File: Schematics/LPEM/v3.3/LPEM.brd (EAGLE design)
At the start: 55.5 x 99.1 mm, 40 parts, among them IC1 7805, IC2 PCA9600SO8, IC3 7803, IC4 7810, Q1 12MHz, U1 STM32F303K8T6, U2 MAX3421E

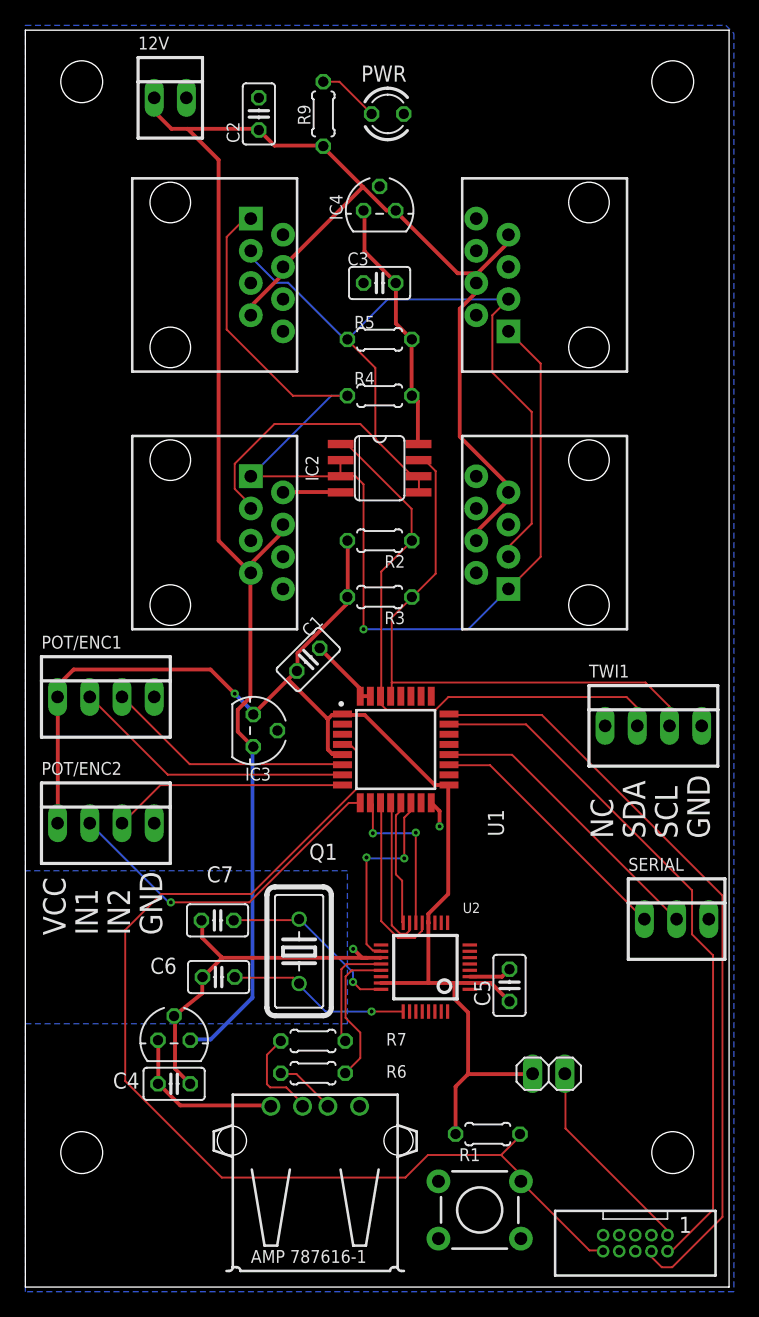
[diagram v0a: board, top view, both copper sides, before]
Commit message: Add LPEM v3.3, which will probably never be produced, and a few cleanups to other files.
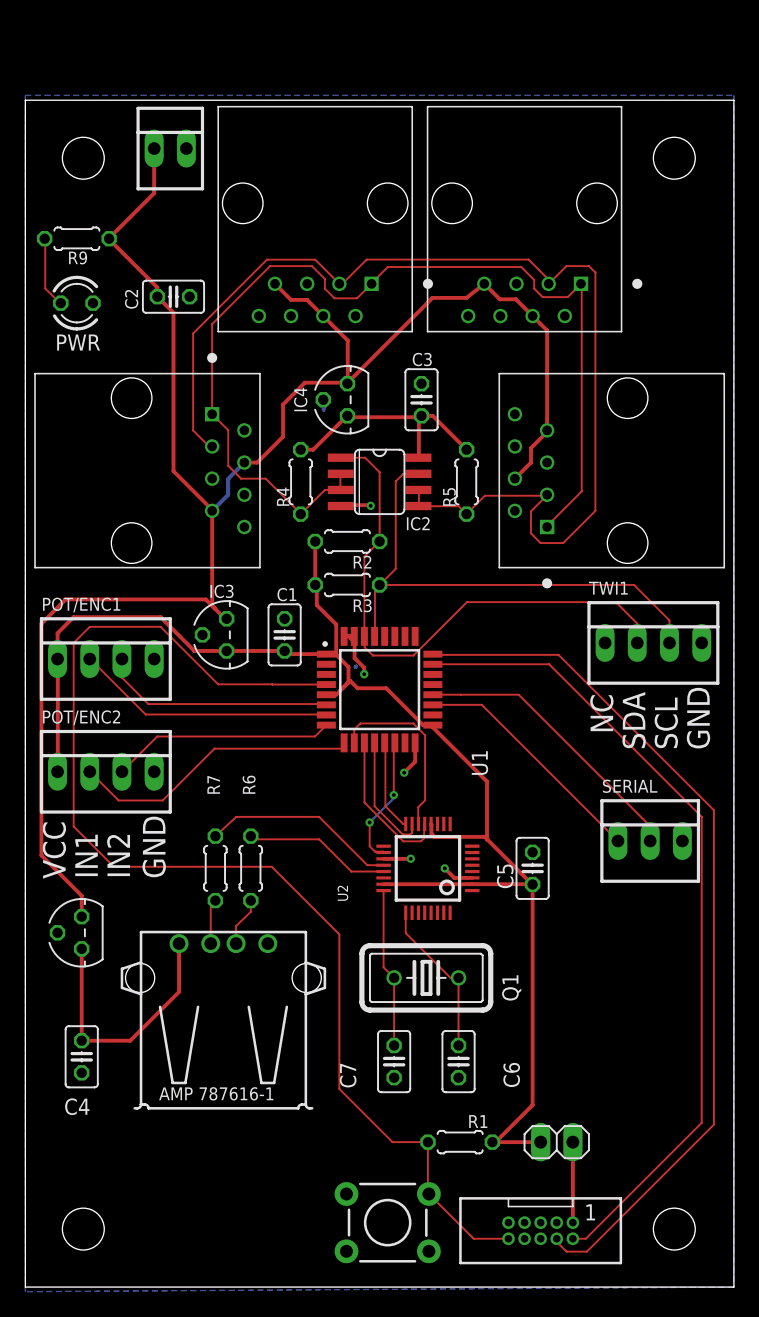
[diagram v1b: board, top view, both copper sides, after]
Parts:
- U$1, U$2, U$3, U$5: value RJ45-8PTH -> 54602-908LF; device SparkFun:RJ45-8 -> 54602-908LF:AMPHENOL_54602-908LF
- moved 5V 28.7 mm to (4.06, 77.6)
- moved R9 21.8 mm to (4.06, 82.7), turned to 0 degrees
- moved C6 20.1 mm to (34.2, 17.8), turned to 270 degrees
- moved C7 17.8 mm to (29.1, 17.8), turned to 270 degrees
- moved R6 16.9 mm to (17.8, 33.0), turned to 270 degrees
- moved C2 15.9 mm to (11.7, 78.1), turned to 0 degrees
- moved R7 15.6 mm to (15.0, 33.0), turned to 270 degrees
- moved IC4 15.1 mm to (25.4, 70.0), turned to 90 degrees
- moved X1 14.7 mm to (15.6, 14.1)
- moved R5 13.2 mm to (34.8, 63.5), turned to 90 degrees
- moved U$3 12.8 mm to (22.9, 85.5), turned to 180 degrees
- moved IC1 11.2 mm to (4.45, 27.9), turned to 90 degrees
- moved Q1 10.2 mm to (31.6, 24.4), turned to 180 degrees
- moved C3 9.78 mm to (31.2, 70.0), turned to 90 degrees
- moved C5 9.40 mm to (40.0, 33.0)
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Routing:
- net GND: track 46.0 -> 15.0 mm, vias 2 -> 5
- net +12V: track 157.5 -> 143.0 mm
- net N$4: track 16.1 -> 6.35 mm
- net SDA_HV: track 88.8 -> 79.9 mm, vias 1 -> 0
- net SCL_HV: track 79.8 -> 88.2 mm
- net SWIO: track 56.1 -> 64.3 mm
- net RESET: track 86.4 -> 94.1 mm
- net SWCLK: track 61.6 -> 69.2 mm
- net +5V: track 13.1 -> 20.3 mm
- net N$12: track 9.17 -> 15.4 mm
- net VCC: track 110.4 -> 116.5 mm, vias 1 -> 0
- net USB_INT: track 15.8 -> 10.3 mm
- net SCL: track 45.2 -> 40.8 mm
- net N$2: track 27.2 -> 23.1 mm, vias 1 -> 0
- net N$8: track 7.51 -> 3.51 mm
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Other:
- board size 55.5 x 99.1 mm -> 55.9 x 93.6 mm
- board text added: "LPEM v3.3 July 2019"
- board text removed: "LPEM v3.2 June 2019"
